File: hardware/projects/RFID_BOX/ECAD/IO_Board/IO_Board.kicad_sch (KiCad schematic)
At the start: 23 parts, among them J1 J_WAGO_2604-1103, J2 J_WAGO_2604-1103, K1 T92S11D12-24, K2 K_G5V-1-2_DC24, U1 ESP32-S3-WROOM-1, U2 PN5321A3HN_C1xx, U3 IC_IRM-10-24, U4 AMS1117-3.3, U5 IC_RFB-0505S, U6 MCP39F511A-E/MQ, U7 VO615A-1, U8 VO615A-1

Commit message: Designator-Umnummerierung IO-Board in README nachziehen, BOM nach Bauteilgruppen gliedern
- README: alle IO-Board-Designatoren (J300, RV300, C300-C306, L300, F300,
  F302, K300, RT300, R300, U300-U306, U304/U305) in Fließtext, beiden
  Mermaid-Diagrammen und der Bauteilauswahl nachgezogen
- Fehlende 3V3_ISO-Versorgungsstrecke (U302 -> U300 -> Lastmessung U303) im
  Power-Distribution-Diagramm ergänzt, Signalfluss-Diagramm entsprechend von
  [5V] auf [3V3] korrigiert
- Neue BOM-Zeilen für bislang nur im Chat recherchierte Stützkondensatoren
  (C301-C306) und den zweiten isolierten 3V3-Regler (U300) ergänzt
- Bauteilauswahl in 8 Kategorien (ICs & Module, Widerstände, Kondensatoren,
  Induktivitäten, Relais & Schutzbeschaltung, Steckverbinder &
  Bedienelemente, Anzeige & Akustik, Sonstige) aufgesplittet
- Datenblätter der recherchierten IO-Board-Bauteile unter docs/Datasheets
  abgelegt
- MCU_Board KiCad-Projekt (Platzierungs-Start) und IO_Board-Fortschritt
- .gitignore um Backup-Ordner des MCU_Board-Pfads ergänzt

Co-Authored-By: Claude Sonnet 5 <noreply@anthropic.com>
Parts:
- removed BZ1: Buzzer, symbol Device:Buzzer
- removed F3: Polyfuse, symbol Device:Polyfuse
- removed unit 1 of K1
- removed K2: K_G5V-1-2_DC24, aa_MyParts:K_G5V-1-2_DC24, symbol aa_MyParts:K_G5V-1-2_DC24
- removed L1: L_CMC_7448258022, aa_MyParts:L_Wurth_WE-CMB-XL, symbol aa_MyParts:L_CMC_7448258022
- removed LED1: LED_IN-PI20TATPRPGPB, aa_MyParts:LED_INPI20TATPRPGPB, symbol aa_MyParts:LED_IN-PI20TATPRPGPB
- removed PS1: IC_R-78K5.0-2.0, aa_MyParts:IC_CONV_R-78K5.0-2.0, symbol aa_MyParts:IC_R-78K5.0-2.0
- removed U1: ESP32-S3-WROOM-1, RF_Module:ESP32-S3-WROOM-1, symbol RF_Module:ESP32-S3-WROOM-1
- removed U2: PN5321A3HN_C1xx, Package_DFN_QFN:HVQFN-40-1EP_6x6mm_P0.5mm_EP4.1x4.1mm, symbol RF_NFC:PN5321A3HN_C1xx
- added C301, C304: 100nF 50V, symbol Device:C
- added C302: 47uF 50V, aa_MyParts:CP_Radial_D6.3mm_H11.0mm_P2.50mm, symbol aa_MyParts:C_Elko_47uF_50V
- added C303: 10uF 10V 0805, symbol Device:C
- added C305, C306: 10uF 10V tantal, symbol Device:C
- added F301: Schurter 0034.3127, symbol Device:Fuse
- added L300: L_CMC_7448258022, aa_MyParts:L_Wurth_WE-CMB-XL, symbol aa_MyParts:L_CMC_7448258022
- added U306: R-78K5.0-2.0, aa_MyParts:IC_CONV_R-78K5.0-2.0, symbol aa_MyParts:IC_R-78K5.0-2.0
- F302: renamed from F2; value 1A 250VAC -> 1AT 250VAC
- R300: renamed from R1; value 20mR -> 2mR PA1206FRM670R002L
- U301: renamed from U3; value IC_IRM-10-24 -> IRM-10-24
- U302: renamed from U5; value IC_RFB-0505S -> RFB-0505S
- renumbered C1 to C300, F1 to F300, J1 to J300, J2 to J301, K1 to K300, TH1 to RT300, RV1 to RV300, U4 to U300, U6 to U303, U8 to U304, U7 to U305
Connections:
- net PIN_L: now also L300.1
- net PIN_N: now also L300.2
- net at U303.25 (DVDD): no longer U300.2 (VO)
- net GND_ISO: now reaches U300.1 (GND), U302.4 (-VOUT), U303.29 (DGND)
- net GND_ISO: now also C304.2, C305.2, C306.2
- net at J301.3 (Pin_3), J301.4 (Pin_4): now also K300.6
- net +5V_ISO: now reaches U300.3 (VI), U302.6 (+VOUT)
- net +5V_ISO: now also C304.1, C305.1
- net PIN_CTRL_L: now reaches F302.2, U301.2 (AC/L)
- net GND: now reaches U301.3 (-Vo), U302.2 (-VIN)
- net GND: now also C301.2, C302.2, C303.2, U306.2 (GND)
- net +24V: now reaches U301.4 (+Vo)
- net +24V: now also C301.1, C302.1, U306.1 (+VIN)
- net +5V: now reaches U302.1 (+VIN)
- net +5V: now also C303.1, U306.3 (+VOUT)
- net PIN_CMC_L renamed PIN_FILTERED_L
- net PIN_FILTERED_L: now also L300.4
- net PIN_CMC_N renamed PIN_FILTERED_N
- net PIN_FILTERED_N: now also L300.3
- new net +3V3_ISO: C306.1, U300.2 (VO)
- no-connect marks 0 -> 2
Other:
- note added: "230V in, Push-in 400V OVC III / 32A V ISO: 4kV"
- note added: "250V 10AT"
- note added: "275VAC 2,5kA (8/20µs)"
- note added: "AC/DC converter In: 85-305VAC Out: 24VDC, 420mA, 10W Eff: 82% Iso: Class II, 4.2kV I/P-O/P Protection: Short-circuit, Overload, Overvoltage"
- note added: "Common Mode Choke"
- note added: "Isolated DC/DC 5V in, 5V out, 200mA, 1W Iso: 500VAC / 1kVDC, 1min Eff: 80%"
- note added: "NTC 2.5R, 8A"
- note added: "Power relay 600VAC, 30A 1P Motor: 1,5HP (~1,1kW)"
- note added: "Shunt"
- note added: "X2-Capacitor"
- note added: "place U306 close to C302 to share bluk capacitor"
- note removed: "230V IN"
- note removed: "DT010ATFT"
- moved on the sheet: C300, F300, F302, J300, RT300, RV300, U300, U301, U302, U303, U304, U305

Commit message: Layout-Regeln ergänzt, Power Distribution überarbeitet, FMEA aufgenommen
Neues Kapitel "Leiterbahnbreiten und Abstände": Stackups der drei Boards,
Breiten- und Via-Tabellen je Board nach IPC-2221 bei ΔT 5 K, Abstandsmatrix
der vier Domänen (Netz, ISO-Insel, SELV, Feld) und die Auslegung des
Messnetzteils.

Vier Korrekturen am I/O-Board, entstanden beim Durchrechnen von Thermik und
Isolationsbarriere:

- RT300 entfällt ersatzlos. Der NTC lag dauerhaft im 8-A-Lastpfad, setzte
  dort ~3 W um und begrenzte beim Wiedereinschalten ohnehin nicht, weil er
  dann noch heiß ist. Den Anlauf tragen F300 (träge) und K300 (30 A, AgCdO).
- Lastmessung sitzt jetzt vor dem Relais statt dahinter. Damit bleibt sie
  unabhängig vom Schaltzustand versorgt und LAST_AUS wird gemessen statt
  aus dem Relaiszustand gefolgert.
- ISO-Insel wird netzseitig über ein Kondensatornetzteil gespeist; U302
  (RFB-0505S) und U300 entfallen. Der RFB-0505S war mit 500 VAC nur
  funktional isoliert und damit das schwächste Glied einer sonst verstärkt
  isolierten Barriere.
- U304 entfällt: die Relaisspule liegt auf SELV, der Optokoppler hätte zwei
  SELV-Domänen getrennt. Der Relaistreiber wird redundant aus
  Low-Side-NMOS und High-Side-PMOS an getrennten GPIOs.

Neues FMEA-Kapitel für die Einzelfehler mit Außenwirkung, mit den daraus
folgenden Maßnahmen: doppelte Z-Diode gegen Ausfall offen, Entladewiderstände
als zwei parallele Reihenpaare, zwei Schalter in Reihe in der Relaisspule.

Anforderungen.md auf Revision 1.5.

Co-Authored-By: Claude Opus 5 <noreply@anthropic.com>
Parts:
- removed RT300: ICL_BN-LG15Y2R5MYB, Varistor:RV_Disc_D15.5mm_W8mm_P7.5mm, symbol aa_MyParts:ICL_BN-LG15Y2R5MYB
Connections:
- net PIN_FUSED_L: now also R300.1, U303.19 (V1+)
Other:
- note removed: "NTC 2.5R, 8A"
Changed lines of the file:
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@@
 		)
 	)
-	(text "NTC\n2.5R, 8A"
-		(exclude_from_sim no)
-		(at 156.21 137.922 0)
-		(effects
-			(font
-				(size 1.27 1.27)
-			)
-		)
-	)
 	(text "Shunt"
 		(exclude_from_sim no)
@@
 	(wire
 		(pts
-			(xy 160.02 148.59) (xy 168.91 148.59)
-		)
-		(stroke
-			(width 0)
-			(type default)
-		)
-	)
-	(wire
-		(pts
 			(xy 182.88 82.55) (xy 177.8 82.55)
 		)
@@
 	(wire
 		(pts
-			(xy 134.62 148.59) (xy 152.4 148.59)
+			(xy 134.62 148.59) (xy 168.91 148.59)
 		)
 		(stroke
@@
 	)
 	(label "PIN_FUSED_L"
-		(at 138.43 148.59 0)
+		(at 144.78 148.59 0)
 		(effects
 			(font
@@
 				)
 			)
-		)
-	)
-	(symbol
-		(lib_id "aa_MyParts:ICL_BN-LG15Y2R5MYB")
-		(at 156.21 148.59 90)
-		(unit 1)
-		(body_style 1)
-		(exclude_from_sim no)
-		(in_bom yes)
-		(on_board yes)
-		(in_pos_files yes)
-		(dnp no)
-		(fields_autoplaced yes)
-		(property "Reference" "RT300"
-			(at 156.5275 142.24 90)
-			(show_name no)
-			(do_not_autoplace no)
-			(effects
-				(font
-					(size 1.27 1.27)
-				)
-			)
-		)
-		(property "Value" "ICL_BN-LG15Y2R5MYB"
-			(at 156.5275 144.78 90)
-			(show_name no)
-			(do_not_autoplace no)
-			(effects
-				(font
-					(size 1.27 1.27)
-				)
-			)
-		)
-		(property "Footprint" "Varistor:RV_Disc_D15.5mm_W8mm_P7.5mm"
-			(at 154.94 148.59 0)
-			(hide yes)
-			(show_name no)
-			(do_not_autoplace no)
-			(effects
-				(font
-					(size 1.27 1.27)
-				)
-			)
-		)
-		(property "Datasheet" ""
-			(at 154.94 148.59 0)
-			(hide yes)
-			(show_name no)
-			(do_not_autoplace no)
-			(effects
-				(font
-					(size 1.27 1.27)
-				)
-			)
-		)
-		(property "Description" "Temperature dependent resistor, negative temperature coefficient"
-			(at 156.21 148.59 0)
-			(hide yes)
-			(show_name no)
-			(do_not_autoplace no)
-			(effects
-				(font
-					(size 1.27 1.27)
-				)
-			)
-		)
-		(pin "1"
-		)
-		(pin "2"
-		)
-		(instances
-			(project "IO_Board"
-				(path "/925169fe-6f55-4c58-8867-9e65957475e7"
-					(reference "RT300")
-					(unit 1)
-				)
-			)

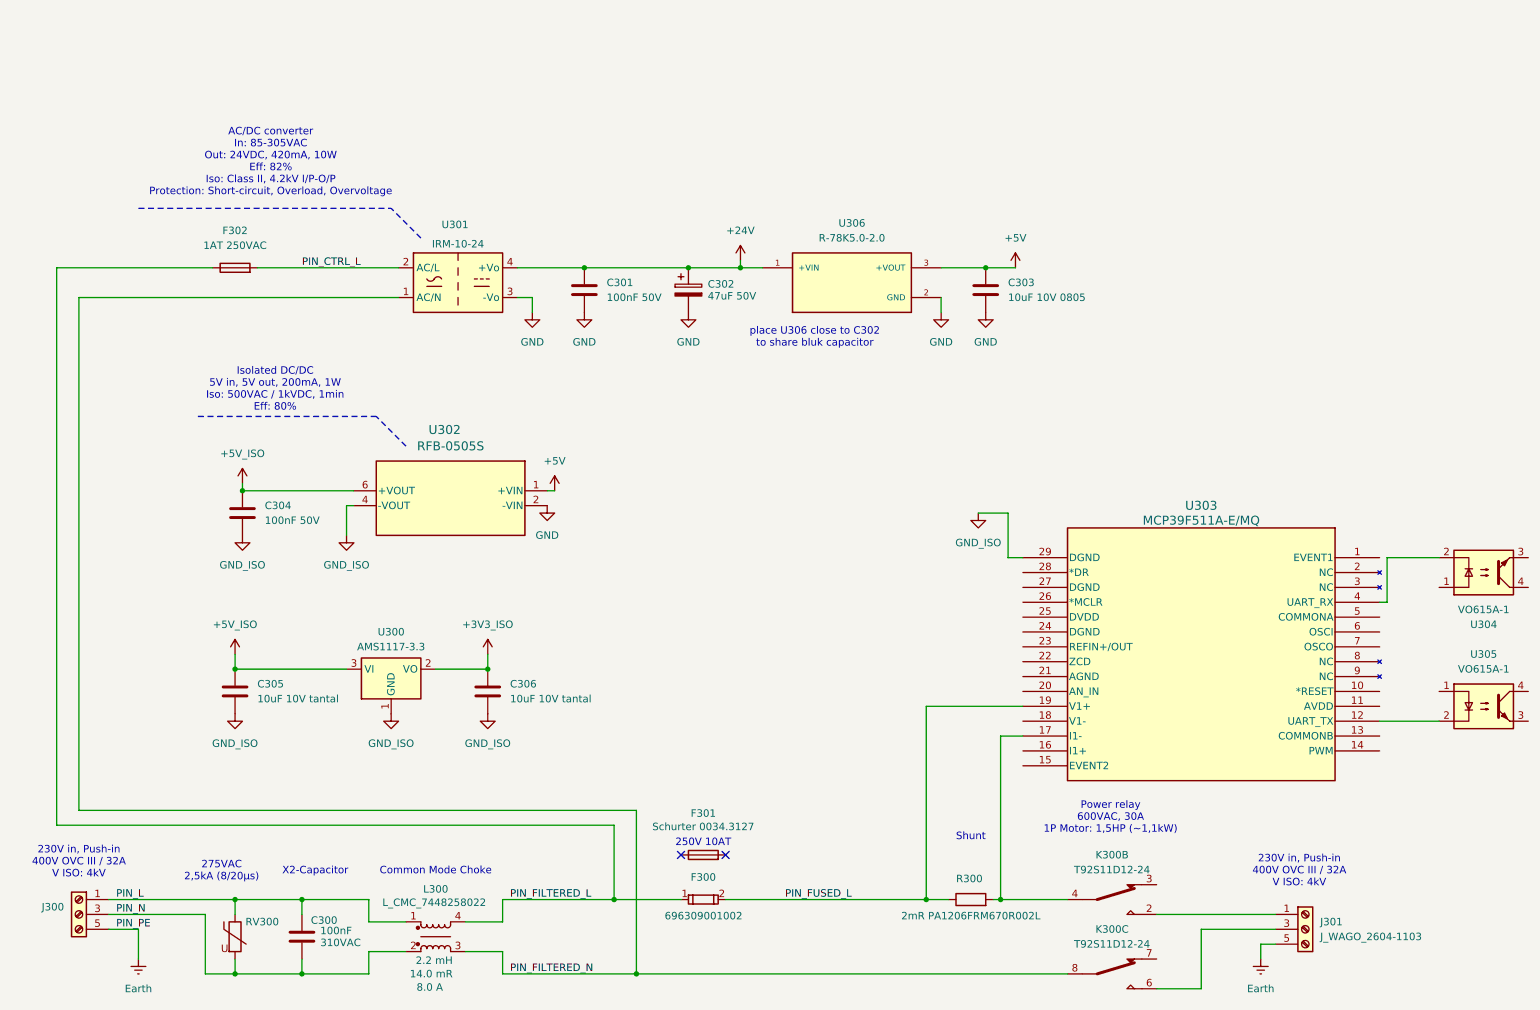
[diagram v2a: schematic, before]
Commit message: Messinsel über isolierten Digitalisolator statt Kondensatornetzteil
Das Kondensatornetzteil der ISO-Messinsel entfällt. Der ISOW7721 (U300)
versorgt sie aus der SELV-Seite und führt zugleich die UART über die
Barriere; er ersetzt damit den LDO U302 und beide Optokoppler U304/U305.
Auslöser war der X2-Vorschaltkondensator, der im Flächenbudget des
I/O-Boards nicht unterzubringen war.

Die 8 mm Luft- und Kriechstrecke kommen jetzt aus dem Bauteil (VDE
0884-17, UL 1577 5 kVrms) statt aus einer Layoutforderung.

Schaltplan: U300 mit Abblockung C307–C317 und Ferriten FB300–FB307,
U302/U304/U305 entfernt.

README: Abschnitt 4 neu gefasst, Power-Distribution-Diagramm korrigiert
(Lastmessung liegt im N-Rückweg, nicht im gesicherten L-Pfad), BOM und
FMEA nachgezogen, U303 auf MCP39F511A-E/MQ berichtigt.

Ausserdem KiCad-Lock- und Autosave-Dateien in .gitignore aufgenommen.

Co-Authored-By: Claude Opus 5 <noreply@anthropic.com>
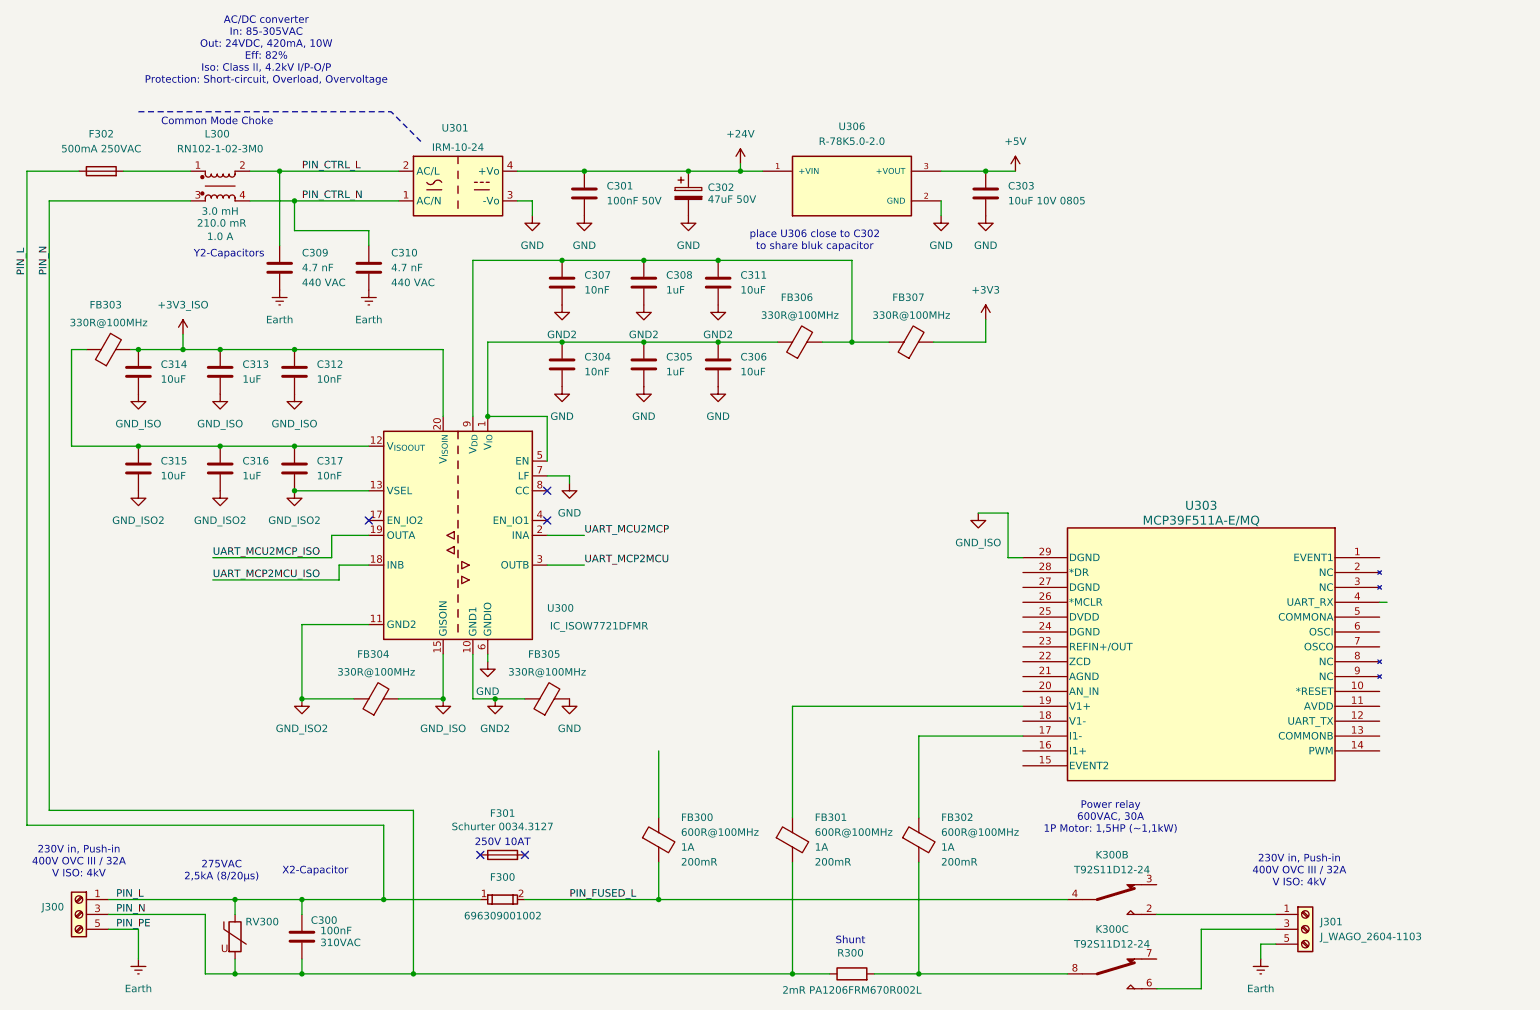
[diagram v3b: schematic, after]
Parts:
- removed F302: 1AT 250VAC, aa_MyParts:F_MRT_BEL, symbol aa_MyParts:F_MRT 1-BULK
- removed L300: L_CMC_7448258022, aa_MyParts:L_Wurth_WE-CMB-XL, symbol aa_MyParts:L_CMC_7448258022
- removed U300: AMS1117-3.3, Package_TO_SOT_SMD:SOT-223-3_TabPin2, symbol Regulator_Linear:AMS1117-3.3
- removed U302: RFB-0505S, aa_MyParts:IC_RFB-0505S, symbol aa_MyParts:IC_RFB-0505S
- removed U304, U305: VO615A-1, Package_DIP:DIP-4_W7.62mm, symbol Isolator:VO615A-1
- added C307, C312, C317: 10nF, symbol Device:C
- added C308, C313, C316: 1uF, symbol Device:C
- added C309, C310: VY2472M49Y5US63L7, Capacitor_THT:C_Disc_D12.5mm_W5.0mm_P7.50mm, symbol aa_MyParts:C_Y2_VY2472M49Y5US63L7
- added C311, C314, C315: 10uF, symbol Device:C
- added F302: 500mA 250VAC, aa_MyParts:F_MRT_BEL, symbol aa_MyParts:F_MRT_500-BULK
- added FB300, FB301, FB302: 600R@100MHz, Inductor_SMD:L_0805_2012Metric, symbol aa_MyParts:L_Ferrite_MH2029-601Y
- added FB303, FB304, FB305, FB306, FB307: 330R@100MHz, Inductor_SMD:L_0805_2012Metric, symbol aa_MyParts:L_Ferrite_MH2029-601Y
- added L300: RN102-1-02-3M0, aa_MyParts:L_RN102_SCN, symbol aa_MyParts:L_CMC_RN102-1-02-3M0
- added U300: IC_ISOW7721DFMR, Package_SO:SOIC-20W_7.5x12.8mm_P1.27mm, symbol aa_MyParts:IC_ISOW7721DFMR
- C304: value 100nF 50V -> 10nF
- C305: value 10uF 10V tantal -> 1uF
- C306: value 10uF 10V tantal -> 10uF
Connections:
- net PIN_FILTERED_L is gone; now on net PIN_L: F300.1
- net +3V3_ISO: now also C312.1, C313.1, C314.1, FB303.2, U300.20 (V_{ISOIN}); no longer C306.1
- net Earth: now also C309.2, C310.2
- net GND: now also C304.2, C305.2, C306.2, FB305.2, U300.6 (GNDIO), U300.7 (LF)
- net GND_ISO: now also C312.2, C313.2, C314.2, FB304.2, U300.15 (GISOIN); no longer C304.2, C305.2, C306.2
- net PIN_CTRL_L: now also C309.1, L300.2
- net PIN_FUSED_L: now also K300.4, FB300.2; no longer R300.1, U303.19 (V1+)
- net PIN_L: now also F302.1
- net PIN_N: now also R300.1, FB301.2, L300.3
- net +5V_ISO: no longer names the net of C304.1, C305.1
- net +5V_ISO: now also C306.1, FB306.1, U300.1 (V_{IO}), U300.5 (EN)
- net PIN_FILTERED_N: no longer names the net of K300.8
- net PIN_FILTERED_N: now also R300.2, FB302.2; no longer U301.1 (AC/N)
- new net: C315.1, C316.1, C317.1, FB303.1, U300.12 (V_{ISOOUT})
- new net: C307.1, C308.1, C311.1, FB306.2, FB307.1, U300.9 (V_{DD})
- new net: FB302.1, U303.17 (I1-)
- new net: FB301.1, U303.19 (V1+)
- new net: F302.2, L300.1
- new net +3V3: FB307.2
- new net GND2: C307.2, C308.2, C311.2, FB305.1, U300.10 (GND1)
- new net GND_ISO2: C315.2, C316.2, C317.2, FB304.1, U300.11 (GND2), U300.13 (VSEL)
- new net PIN_CTRL_N: C310.1, L300.4, U301.1 (AC/N)
- new net UART_MCP2MCU: U300.3 (OUTB)
- new net UART_MCP2MCU_ISO: U300.18 (INB)
- new net UART_MCU2MCP: U300.2 (INA)
- new net UART_MCU2MCP_ISO: U300.19 (OUTA)
- no-connect marks 2 -> 5
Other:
- note added: "Y2-Capacitors"
- note removed: "Isolated DC/DC 5V in, 5V out, 200mA, 1W Iso: 500VAC / 1kVDC, 1min Eff: 80%"
- moved on the sheet: C301, C302, C303, F300, F301, R300, U301, U306
